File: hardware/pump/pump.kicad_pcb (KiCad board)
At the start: 2 copper layers, 47.6 x 38.7 mm, 14 parts, among them J1 DB9_Male, J2 GroupheadThermistor, J3 PumpThermistor, J4 PumpConnect, J5 HeaterRelayConnect, K1 G3MC202PDC5

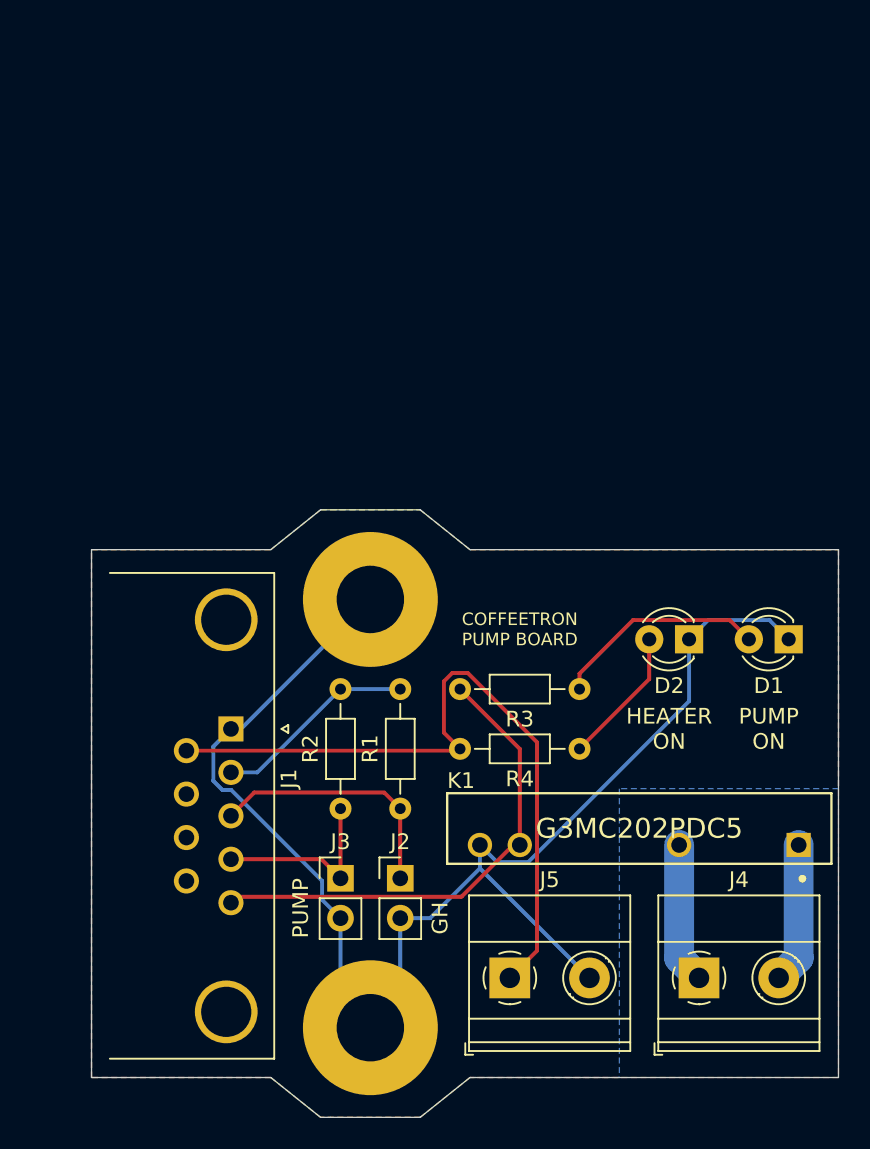
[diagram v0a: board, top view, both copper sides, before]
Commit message: Rework pump hardware based on experimentation
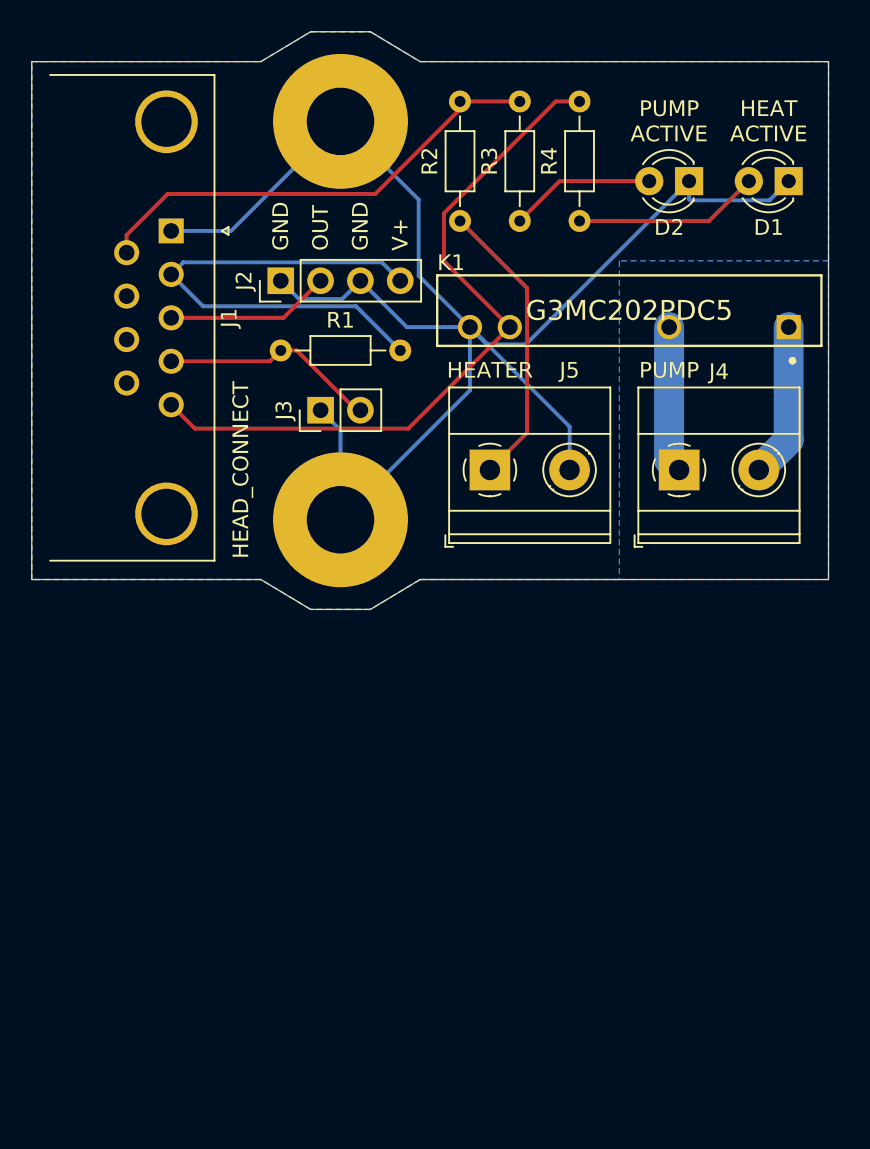
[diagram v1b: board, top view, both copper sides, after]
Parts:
- J2: value GroupheadThermistor -> PumpThermocoupleAdc; footprint Connector_PinHeader_2.54mm:PinHeader_1x02_P2.54mm_Vertical -> Connector_PinHeader_2.54mm:PinHeader_1x04_P2.54mm_Vertical
- J3: value PumpThermistor -> GroupheadThermistor
- R2: value 10000 -> 680
- moved H1 57.8 mm to (90.8, 67.9)
- moved J2 38.9 mm to (87.0, 78.1), turned to 90 degrees
- moved R2 38.2 mm to (98.4, 74.3)
- moved R4 33.7 mm to (106.0, 74.3), turned to 90 degrees
- moved K1 33.0 mm to (109.2, 80.0)
- moved J4 32.4 mm to (112.4, 90.2)
- moved J5 32.4 mm to (100.3, 90.2)
- moved J1 32.0 mm to (80.0, 74.9)
- moved R1 30.2 mm to (87.0, 82.5), turned to 0 degrees
- moved R3 30.1 mm to (102.2, 74.3), turned to 90 degrees
- moved J3 29.9 mm to (89.5, 86.4), turned to 90 degrees
- moved D1 29.2 mm to (119.4, 71.8)
- moved D2 29.2 mm to (113.0, 71.8)
- moved H2 5.43 mm to (90.8, 93.3)
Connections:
- J2 pad 1: PUMP_TEMP -> GND
- J2 pad 2: GND -> PUMP_TEMP
- J3 pad 1: GH_TEMP -> GND
- J3 pad 2: GND -> GH_TEMP
- J5 pad 1: HEATER_RELAY -> Net-(J5-Pad1)
- R1 pad 1: PUMP_TEMP -> GH_TEMP
- R2 pad 1: GH_TEMP -> Net-(J5-Pad1)
- R2 pad 2: +5V -> HEATER_RELAY
- R3 pad 1: Net-(D1-Pad2) -> Net-(D2-Pad2)
- R3 pad 2: PUMP -> HEATER_RELAY
- R4 pad 1: Net-(D2-Pad2) -> Net-(D1-Pad2)
- R4 pad 2: HEATER_RELAY -> PUMP
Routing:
- net +5V: track 13.0 -> 32.0 mm
- net Net-(J5-Pad1): track 0.00 -> 18.6 mm
- net HEATER_RELAY: track 45.9 -> 30.0 mm
- net GND: track 91.2 -> 106.2 mm
- net PUMP: track 31.5 -> 45.5 mm
- net PUMP_TEMP: track 16.3 -> 10.5 mm
- net GH_TEMP: track 11.9 -> 13.9 mm
- net Net-(D1-Pad2): track 13.7 -> 11.8 mm
- net Net-(J4-Pad2): track 9.00 -> 9.90 mm
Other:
- board size 47.6 x 38.7 mm -> 50.8 x 36.8 mm
- board text added: "GND"
- board text added: "HEAD_CONNECT"
- board text added: "HEAT ACTIVE"
- board text added: "HEATER"
- board text added: "OUT"
- board text added: "PUMP ACTIVE"
- board text added: "V+"
- board text removed: "COFFEETRON PUMP BOARD"
- board text removed: "GH"
- board text removed: "HEATER ON"
- board text removed: "PUMP ON"
